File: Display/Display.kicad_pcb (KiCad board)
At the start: 2 copper layers, 163 x 48 mm, 6 parts

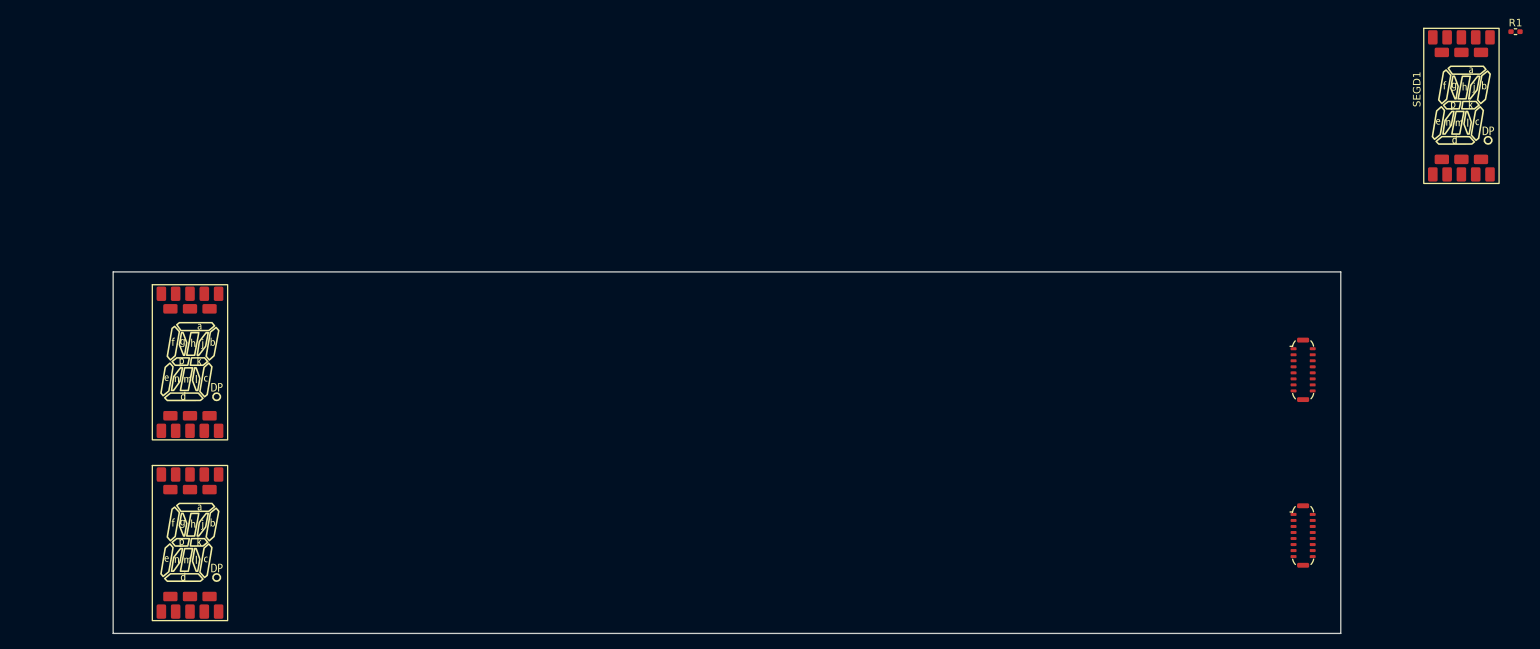
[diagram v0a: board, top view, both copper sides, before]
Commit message: some placeholders ought to be replaced
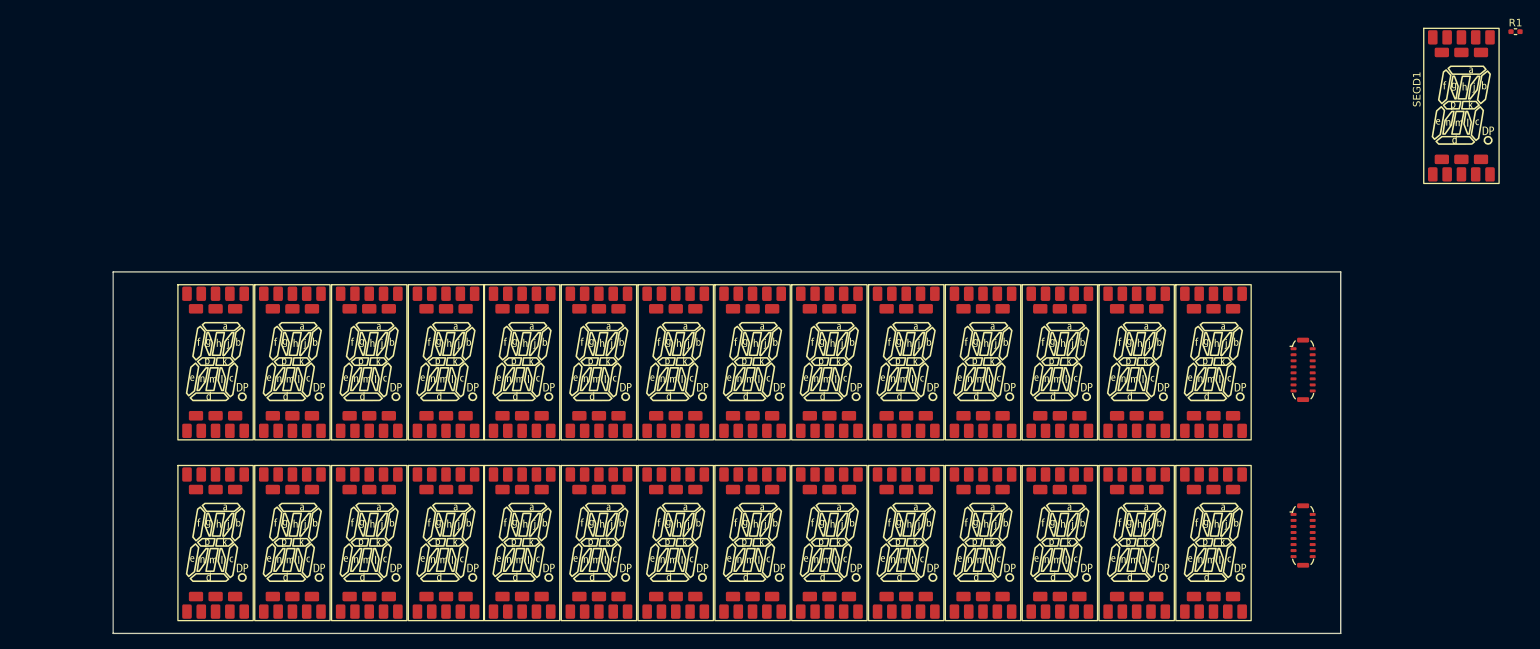
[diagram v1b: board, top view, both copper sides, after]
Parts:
- added REF**: ACPSC04-41SEKWA, External_Parts:ACPSC04-41SEKWA, F.Cu at (129.3, 102.0)
- added REF**: ACPSC04-41SEKWA, External_Parts:ACPSC04-41SEKWA, F.Cu at (159.9, 102.0)
- added REF**: ACPSC04-41SEKWA, External_Parts:ACPSC04-41SEKWA, F.Cu at (221.1, 102.0)
- added REF**: ACPSC04-41SEKWA, External_Parts:ACPSC04-41SEKWA, F.Cu at (149.7, 78.0)
- added REF**: ACPSC04-41SEKWA, External_Parts:ACPSC04-41SEKWA, F.Cu at (221.1, 78.0)
- added REF**: ACPSC04-41SEKWA, External_Parts:ACPSC04-41SEKWA, F.Cu at (210.9, 102.0)
- added REF**: ACPSC04-41SEKWA, External_Parts:ACPSC04-41SEKWA, F.Cu at (139.5, 78.0)
- added REF**: ACPSC04-41SEKWA, External_Parts:ACPSC04-41SEKWA, F.Cu at (210.9, 78.0)
- added REF**: ACPSC04-41SEKWA, External_Parts:ACPSC04-41SEKWA, F.Cu at (180.3, 78.0)
- added REF**: ACPSC04-41SEKWA, External_Parts:ACPSC04-41SEKWA, F.Cu at (170.1, 78.0)
- added REF**: ACPSC04-41SEKWA, External_Parts:ACPSC04-41SEKWA, F.Cu at (170.1, 102.0)
- added REF**: ACPSC04-41SEKWA, External_Parts:ACPSC04-41SEKWA, F.Cu at (200.7, 78.0)
- added REF**: ACPSC04-41SEKWA, External_Parts:ACPSC04-41SEKWA, F.Cu at (129.3, 78.0)
- added REF**: ACPSC04-41SEKWA, External_Parts:ACPSC04-41SEKWA, F.Cu at (98.8, 78.0)
- added REF**: ACPSC04-41SEKWA, External_Parts:ACPSC04-41SEKWA, F.Cu at (200.7, 102.0)
- added REF**: ACPSC04-41SEKWA, External_Parts:ACPSC04-41SEKWA, F.Cu at (98.8, 102.0)
- added REF**: ACPSC04-41SEKWA, External_Parts:ACPSC04-41SEKWA, F.Cu at (109.0, 102.0)
- added REF**: ACPSC04-41SEKWA, External_Parts:ACPSC04-41SEKWA, F.Cu at (109.0, 78.0)
- added REF**: ACPSC04-41SEKWA, External_Parts:ACPSC04-41SEKWA, F.Cu at (149.7, 102.0)
- added REF**: ACPSC04-41SEKWA, External_Parts:ACPSC04-41SEKWA, F.Cu at (119.2, 78.0)
- added REF**: ACPSC04-41SEKWA, External_Parts:ACPSC04-41SEKWA, F.Cu at (139.5, 102.0)
- added REF**: ACPSC04-41SEKWA, External_Parts:ACPSC04-41SEKWA, F.Cu at (190.5, 78.0)
- added REF**: ACPSC04-41SEKWA, External_Parts:ACPSC04-41SEKWA, F.Cu at (180.3, 102.0)
- added REF**: ACPSC04-41SEKWA, External_Parts:ACPSC04-41SEKWA, F.Cu at (119.2, 102.0)
- added REF**: ACPSC04-41SEKWA, External_Parts:ACPSC04-41SEKWA, F.Cu at (190.5, 102.0)
- added REF**: ACPSC04-41SEKWA, External_Parts:ACPSC04-41SEKWA, F.Cu at (159.9, 78.0)
- moved REF** 3.40 mm to (88.6, 78.0)
- moved REF** 3.40 mm to (88.6, 102.0)

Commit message: user save. too many dispalys
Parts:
- removed R1: 100, Resistor_SMD:R_0402_1005Metric_Pad0.72x0.64mm_HandSolder
- removed the REF** at (129.3, 102.0)
- removed the REF** at (159.9, 102.0)
- removed the REF** at (221.1, 102.0)
- removed the REF** at (149.7, 78.0)
- removed the REF** at (221.1, 78.0)
- removed the REF** at (210.9, 102.0)
- removed the REF** at (139.5, 78.0)
- removed the REF** at (88.6, 78.0)
- removed the REF** at (210.9, 78.0)
- removed the REF** at (180.3, 78.0)
- removed the REF** at (170.1, 78.0)
- removed the REF** at (170.1, 102.0)
- removed the REF** at (200.7, 78.0)
- removed the REF** at (129.3, 78.0)
- removed the REF** at (98.8, 78.0)
- removed the REF** at (200.7, 102.0)
- removed the REF** at (88.6, 102.0)
- removed the REF** at (98.8, 102.0)
- removed the REF** at (109.0, 102.0)
- removed the REF** at (109.0, 78.0)
- removed the REF** at (149.7, 102.0)
- removed the REF** at (119.2, 78.0)
- removed the REF** at (139.5, 102.0)
- removed the REF** at (190.5, 78.0)
- removed the REF** at (180.3, 102.0)
- removed the REF** at (119.2, 102.0)
- removed the REF** at (190.5, 102.0)
- removed the REF** at (159.9, 78.0)
- removed SEGD1: ~, External_Parts:ACPSC04-41SEKWA

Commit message: before routing
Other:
- board size 163 x 48 mm -> 176 x 48 mm
- board text removed: "Schlitz, der noch nicht kontrolliert wurde, ob er lang und breit genug ist"
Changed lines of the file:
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@@
 	)
 	(gr_rect
-		(start 75 66)
+		(start 62 66)
 		(end 238 114)
 		(stroke
@@
 	)
 	(gr_rect
-		(start 62.2 84.85)
-		(end 80.2 95.15)
-		(stroke
-			(width 0.1)
-			(type default)
-		)
-		(fill no)
-		(layer "B.Fab")
-	)
-	(gr_rect
-		(start 62.2 89.25)
-		(end 80.2 90.75)
+		(start 97.95 120.5)
+		(end 108.25 102.5)
+		(stroke
+			(width 0.1)
+			(type default)
+		)
+		(fill no)
+		(layer "B.Fab")
+	)
+	(gr_rect
+		(start 102.35 120.5)
+		(end 103.85 102.5)
 		(stroke
 			(width 0.1)
@@
 	)
 	(gr_rect
-		(start 61.7 65)
-		(end 80.7 115)
-		(stroke
-			(width 0.1)
-			(type default)
-		)
-		(fill no)
-		(layer "B.Fab")
-	)
-	(gr_rect
-		(start 68.7 67)
-		(end 73.7 113)
-		(stroke
-			(width 0.1)
-			(type default)
-		)
-		(fill no)
-		(layer "B.Fab")
-	)
-	(gr_rect
-		(start 62.2 82.65)
-		(end 80.2 97.35)
+		(start 78.1 121)
+		(end 128.1 102)
+		(stroke
+			(width 0.1)
+			(type default)
+		)
+		(fill no)
+		(layer "B.Fab")
+	)
+	(gr_rect
+		(start 80.1 114)
+		(end 126.1 109)
+		(stroke
+			(width 0.1)
+			(type default)
+		)
+		(fill no)
+		(layer "B.Fab")
+	)
+	(gr_rect
+		(start 95.75 120.5)
+		(end 110.45 102.5)
 		(stroke
 			(width 0.1)
@@
 		(start 61 71.5)
 		(end 44.2 80)
-		(stroke
-			(width 0.1)
-			(type default)
-		)
-		(layer "F.Fab")
-	)
-	(gr_line
-		(start 71.2 67)
-		(end 86.4 36.6)
 		(stroke
 			(width 0.1)
@@
 			)
 			(justify right bottom)
-		)
-	)
-	(gr_text "Schlitz, der noch nicht kontrolliert wurde, ob er lang und breit genug ist"
-		(at 86.4 36.6 0)
-		(layer "F.Fab")
-		(effects
-			(font
-				(size 1 1)
-				(thickness 0.15)
-			)
-			(justify left bottom)
 		)
 	)
@@
 			(keep_text_aligned yes)
 		)
-		(gr_text "1.7"
+		(gr_text "1,7"
 			(at 246.9 64.1 90)
 			(layer "F.Fab")
@@
 			(keep_text_aligned yes)
 		)
-		(gr_text "1.7"
+		(gr_text "1,7"
 			(at 247.6 110.5 90)
 			(layer "F.Fab")
